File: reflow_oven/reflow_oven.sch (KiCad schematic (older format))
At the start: 30 parts, among them J1 UART, J2 POWER, J3 LED, J4 K-TYPE, J5 BUTTON1, J6 BUTTON2, J7 RELAY, J8 I2C, Q1 2n2222, U1 ATmega328-PU, U2 MAX6675, Y1 16MHz

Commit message: Updated Design
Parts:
- added C10: 100n, Capacitor_SMD:C_0805_2012Metric, symbol Device:C_Small
- added D1: MBR0540T1G, Diode_SMD:D_SOD-123, symbol Device:D_ALT
- added J10: FAN, Connector_Molex:Molex_KK-254_AE-6410-02A_1x02_P2.54mm_Vertical, symbol Connector:Conn_01x02_Male
- added J9: BUTTON3, Connector_Molex:Molex_KK-254_AE-6410-02A_1x02_P2.54mm_Vertical, symbol Connector:Conn_01x02_Male
- added Q2: 2n2222, Package_TO_SOT_THT:TO-92_Inline, symbol Transistor_BJT:BC517
- added R6, R7: 1k, Resistor_SMD:R_0805_2012Metric, symbol Device:R
- J1, J8: footprint Connector_Molex:Molex_KK-396_A-41791-0004_1x04_P3.96mm_Vertical -> Connector_Molex:Molex_KK-254_AE-6410-04A_1x04_P2.54mm_Vertical
- J2, J3, J4, J5, J6, J7: footprint Connector_Molex:Molex_KK-396_A-41791-0002_1x02_P3.96mm_Vertical -> Connector_Molex:Molex_KK-254_AE-6410-02A_1x02_P2.54mm_Vertical
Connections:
- net +5V: now also J7.1 (Pin_1), J8.1 (Pin_1), D1.1 (K), J10.2 (Pin_2); no longer J8.3 (Pin_3)
- net GND: now also C10.2, J9.2 (Pin_2), Q2.3 (E); no longer J7.2 (Pin_2)
- net RELAY_CONN: now also J7.2 (Pin_2); no longer J7.1 (Pin_1)
- net RST: now also J1.3 (Pin_3); no longer J1.1 (Pin_1)
- net SCL: now also J8.3 (Pin_3); no longer J8.2 (Pin_2)
- net SDA: now also J8.2 (Pin_2); no longer J8.1 (Pin_1)
- net UART_TX: now also J1.1 (Pin_1); no longer J1.3 (Pin_3)
- net FAN: now reaches U1.23 (PC0)
- net FAN: now also R7.2
- net BUTTON3: now reaches U1.6 (PD4)
- net BUTTON3: now also C10.1, R6.2
- new net: Q2.2 (B), R7.1
- new net BUTTON3_CONN: J9.1 (Pin_1), R6.1
- new net FAN_CONN-: D1.2 (A), J10.1 (Pin_1), Q2.1 (C)
- no-connect marks 10 -> 8
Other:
- moved on the sheet: C7, C8, C9, H1, H2, H3, H4, J4, J5, J6, J8, Q1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

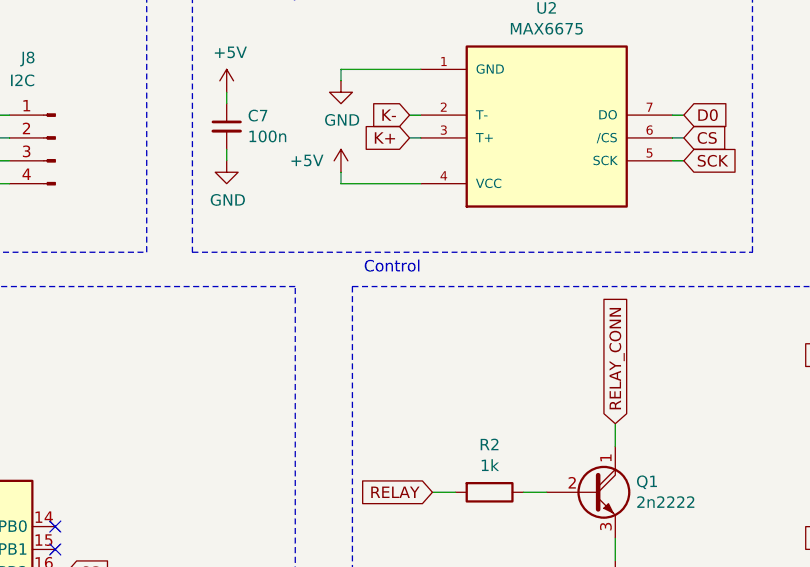
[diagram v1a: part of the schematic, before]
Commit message: Added SMD Crystal
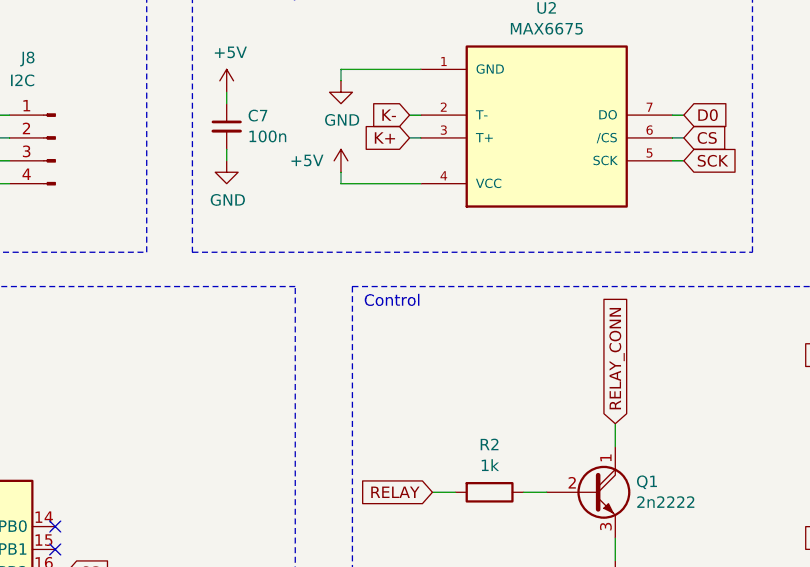
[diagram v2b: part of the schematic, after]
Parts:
- Y1: footprint Crystal:Crystal_SMD_0603-2Pin_6.0x3.5mm_HandSoldering -> Crystal:Crystal_SMD_HC49-SD
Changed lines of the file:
@@
 F 0 "Y1" V 1650 6150 50  0000 C CNN
 F 1 "16MHz" V 1550 6150 50  0000 C CNN
-F 2 "Crystal:Crystal_SMD_0603-2Pin_6.0x3.5mm_HandSoldering" H 1600 6400 50  0001 C CNN
+F 2 "Crystal:Crystal_SMD_HC49-SD" H 1600 6400 50  0001 C CNN
 F 3 "~" H 1600 6400 50  0001 C CNN
 	1    1600 6400
@@
 Text Notes 4200 1950 0    50   ~ 0
 Thermocouple
-Text Notes 4900 3150 0    50   ~ 0
+Text Notes 4900 3300 0    50   ~ 0
 Control
 Wire Notes Line

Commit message: Fina ldesign
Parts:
- added D2: ONLED, LED_SMD:LED_1206_3216Metric, symbol Device:LED_ALT
- added R8: 330, Resistor_SMD:R_0805_2012Metric, symbol Device:R
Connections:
- net +5V: now also R8.1
- net GND: now also D2.1 (K)
- new net: D2.2 (A), R8.2
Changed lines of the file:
@@
 Wire Wire Line
 	2250 900  2250 850
+$Comp
+L Device:LED_ALT D2
+U 1 1 6065D63C
+P 1550 5000
+F 0 "D2" H 1543 4745 50  0000 C CNN
+F 1 "ONLED" H 1543 4836 50  0000 C CNN
+F 2 "LED_SMD:LED_1206_3216Metric" H 1550 5000 50  0001 C CNN
+F 3 "~" H 1550 5000 50  0001 C CNN
+	1    1550 5000
+	-1   0    0    1
+$EndComp
+$Comp
+L Device:R R8
+U 1 1 6065E5AE
+P 1150 5000
+F 0 "R8" V 1357 5000 50  0000 C CNN
+F 1 "330" V 1266 5000 50  0000 C CNN
+F 2 "Resistor_SMD:R_0805_2012Metric" V 1080 5000 50  0001 C CNN
+F 3 "~" H 1150 5000 50  0001 C CNN
+	1    1150 5000
+	0    -1   -1   0
+$EndComp
+Wire Wire Line
+	900  5000 1000 5000
+Wire Wire Line
+	900  5000 900  4950
+Wire Wire Line
+	1300 5000 1400 5000
+Wire Wire Line
+	1700 5000 1800 5000
+Wire Wire Line
+	1800 5000 1800 5050
+$Comp
+L power:+5V #PWR028
+U 1 1 60684AF8
+P 900 4950
+F 0 "#PWR028" H 900 4800 50  0001 C CNN
+F 1 "+5V" H 915 5123 50  0000 C CNN
+F 2 "" H 900 4950 50  0001 C CNN
+F 3 "" H 900 4950 50  0001 C CNN
+	1    900  4950
+	1    0    0    -1
+$EndComp
+$Comp
+L power:GND #PWR029
+U 1 1 60685E94
+P 1800 5050
+F 0 "#PWR029" H 1800 4800 50  0001 C CNN
+F 1 "GND" H 1805 4877 50  0000 C CNN
+F 2 "" H 1800 5050 50  0001 C CNN
+F 3 "" H 1800 5050 50  0001 C CNN
+	1    1800 5050
+	1    0    0    -1
+$EndComp
 $EndSCHEMATC
